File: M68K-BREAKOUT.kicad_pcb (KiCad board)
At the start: 4 copper layers, 27 parts, among them U1 68010D, U2 74ALVC164245, U3 74ALVC164245, U4 74ALVC164245, U5 74ALVC164245, U6 74LVC06

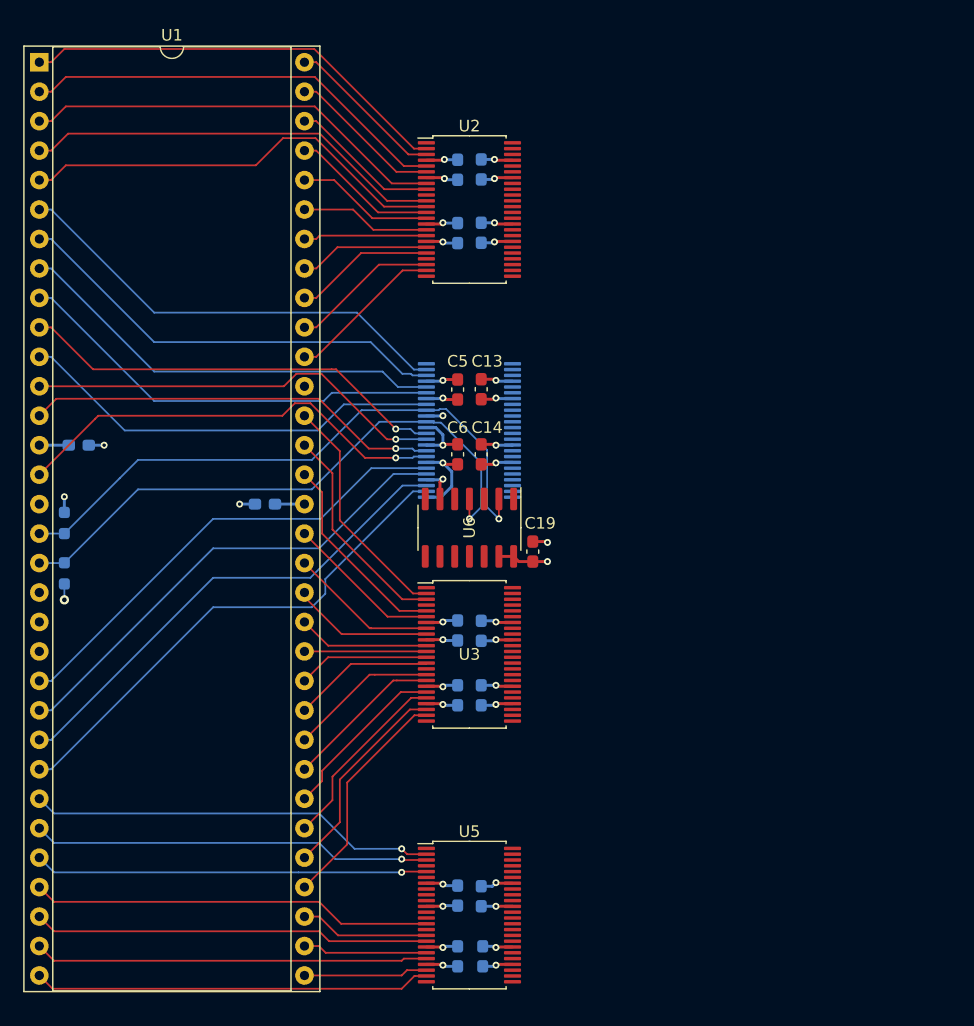
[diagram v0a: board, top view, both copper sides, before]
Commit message: complete electrical layout for the silicon centipede charmer
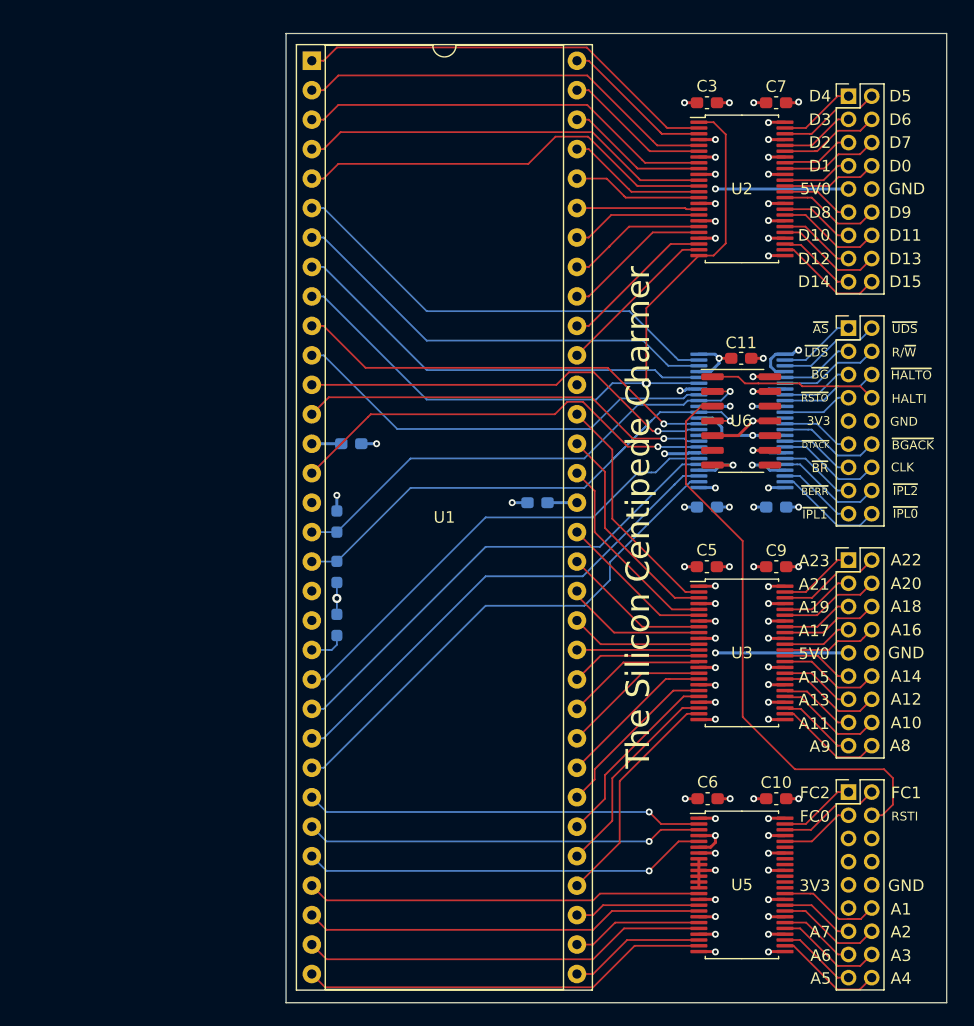
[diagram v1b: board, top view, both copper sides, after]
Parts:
- removed C12, C13, C14, C15, C16, C17, C18, C19: 100nF, Capacitor_SMD:C_0603_1608Metric_Pad1.08x0.95mm_HandSolder
- added J1: Data, Connector_PinHeader_2.00mm:PinHeader_2x09_P2.00mm_Vertical, F.Cu at (171.2, 61.1)
- added J2: Bus Signals, Connector_PinHeader_2.00mm:PinHeader_2x09_P2.00mm_Vertical, F.Cu at (171.2, 81.1)
- added J3: Address, Connector_PinHeader_2.00mm:PinHeader_2x09_P2.00mm_Vertical, F.Cu at (171.2, 101.1)
- added J4: Function Code and Lower Address, Connector_PinHeader_2.00mm:PinHeader_2x09_P2.00mm_Vertical, F.Cu at (171.2, 121.1)
- added R3: 2.2K, Resistor_SMD:R_0603_1608Metric_Pad0.98x0.95mm_HandSolder, B.Cu at (127.1, 106.7)
- C10, C11, C3, C7, C9: moved to F.Cu
- moved C7 53.1 mm to (165.0, 61.7), turned to 180 degrees
- moved C9 39.5 mm to (165.0, 101.7), turned to 180 degrees
- moved C6 36.7 mm to (159.1, 121.7), turned to 0 degrees
- moved C4 31.9 mm to (159.0, 96.5), turned to 0 degrees
- moved C8 31.9 mm to (165.0, 96.5), turned to 180 degrees
- moved C10 30.6 mm to (165.0, 121.7), turned to 180 degrees
- moved C11 27.7 mm to (162.0, 83.7), turned to 180 degrees
- moved C5 26.4 mm to (159.0, 101.7), turned to 0 degrees
- moved U6 25.2 mm to (162.0, 89.1), turned to 0 degrees
- moved U5 23.6 mm to (162.1, 129.1)
- moved U2 23.6 mm to (162.1, 69.1)
- moved U4 23.5 mm to (162.1, 89.1)
- moved C2 23.5 mm to (144.4, 96.1)
- moved U1 23.5 mm to (125.0, 58.0)
- moved U3 23.5 mm to (162.1, 109.1)
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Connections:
- C10 pad 1: +5V -> +3V3
- C7 pad 1: +5V -> +3V3
- C8 pad 1: +5V -> +3V3
- C9 pad 1: +5V -> +3V3
- U1 pad 21: +5V -> Net-(R3-Pad2)
- U2 pad 26: Net-(U2-Pad26) -> DD15
- U2 pad 27: Net-(U2-Pad27) -> DD14
- U2 pad 29: Net-(U2-Pad29) -> DD13
- U2 pad 30: Net-(U2-Pad30) -> DD12
- U2 pad 32: Net-(U2-Pad32) -> DD11
- U2 pad 33: Net-(U2-Pad33) -> DD10
- U2 pad 35: Net-(U2-Pad35) -> DD9
- U2 pad 36: Net-(U2-Pad36) -> DD8
- U2 pad 37: Net-(U2-Pad37) -> DD0
- U2 pad 38: Net-(U2-Pad38) -> DD1
- U2 pad 40: Net-(U2-Pad40) -> DD7
- U2 pad 41: Net-(U2-Pad41) -> DD2
- U2 pad 43: Net-(U2-Pad43) -> DD6
- U2 pad 44: Net-(U2-Pad44) -> DD3
- U2 pad 46: Net-(U2-Pad46) -> DD5
- U2 pad 47: Net-(U2-Pad47) -> DD4
- U3 pad 26: Net-(U3-Pad26) -> AA8
- U3 pad 27: Net-(U3-Pad27) -> AA9
- U3 pad 29: Net-(U3-Pad29) -> AA10
- U3 pad 30: Net-(U3-Pad30) -> AA11
- U3 pad 32: Net-(U3-Pad32) -> AA12
- U3 pad 33: Net-(U3-Pad33) -> AA13
- U3 pad 35: Net-(U3-Pad35) -> AA14
- U3 pad 36: Net-(U3-Pad36) -> AA15
- U3 pad 37: Net-(U3-Pad37) -> AA16
- U3 pad 38: Net-(U3-Pad38) -> AA17
- U3 pad 40: Net-(U3-Pad40) -> AA18
- U3 pad 41: Net-(U3-Pad41) -> AA19
- U3 pad 43: Net-(U3-Pad43) -> AA20
- U3 pad 44: Net-(U3-Pad44) -> AA21
- U3 pad 46: Net-(U3-Pad46) -> AA22
- U3 pad 47: Net-(U3-Pad47) -> AA23
- U4 pad 26: Net-(U4-Pad26) -> ~L_AS
- U4 pad 27: Net-(U4-Pad27) -> ~L_UDS
- U4 pad 29: Net-(U4-Pad29) -> ~L_LDS
- U4 pad 30: Net-(U4-Pad30) -> L_R~W
- U4 pad 32: Net-(U4-Pad32) -> ~L_BG
- U4 pad 33: Net-(U4-Pad33) -> ~L_HALT
- U4 pad 35: Net-(U4-Pad35) -> ~L_RESET
- U4 pad 36: GND -> Net-(U4-Pad36)
- U4 pad 37: Net-(U4-Pad37) -> ~L_DTACK
- U4 pad 38: Net-(U4-Pad38) -> ~L_BGACK
- U4 pad 40: Net-(U4-Pad40) -> ~L_BR
- U4 pad 41: Net-(U4-Pad41) -> L_CLK
- U4 pad 43: Net-(U4-Pad43) -> ~L_BERR
- U4 pad 44: Net-(U4-Pad44) -> ~L_IPL2
- U4 pad 46: Net-(U4-Pad46) -> ~L_IPL1
- U4 pad 47: Net-(U4-Pad47) -> ~L_IPL0
- U5 pad 26: LA4 -> AA4
- U5 pad 27: LA5 -> AA5
- U5 pad 29: LA3 -> AA3
- U5 pad 30: LA6 -> AA6
- U5 pad 32: LA2 -> AA2
- U5 pad 33: LA7 -> AA7
- U5 pad 35: LA1 -> AA1
- U5 pad 36: GND -> Net-(U5-Pad36)
- U5 pad 37: GND -> Net-(U5-Pad37)
- U5 pad 38: GND -> Net-(U5-Pad38)
- U5 pad 40: GND -> Net-(U5-Pad40)
- U5 pad 41: GND -> Net-(U5-Pad41)
- U5 pad 43: GND -> Net-(U5-Pad43)
- U6 pad 1: ~HALT_IN -> HALT_IN
- U6 pad 10: GND -> Net-(U6-Pad10)
- U6 pad 12: GND -> Net-(U6-Pad12)
- U6 pad 3: ~RESET_IN -> RESET_IN
- U6 pad 6: GND -> Net-(U6-Pad6)
- U6 pad 8: GND -> Net-(U6-Pad8)
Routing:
- net RESET_IN: track 0.00 -> 50.0 mm
- net GND: track 55.0 -> 100.3 mm, vias 21 -> 52
- net R~W: track 37.3 -> 65.4 mm, vias 0 -> 1
- net +5V: track 34.9 -> 51.2 mm, vias 10 -> 17
- net HALT_IN: track 0.00 -> 14.5 mm
- net ~L_UDS: track 0.00 -> 10.7 mm
- net ~HALT: track 52.6 -> 42.6 mm
- net AA1: track 0.00 -> 9.84 mm
- net AA4: track 0.00 -> 9.46 mm
- net ~L_IPL0: track 0.00 -> 9.46 mm
- net DD15: track 0.00 -> 9.46 mm
- net AA8: track 0.00 -> 9.44 mm
- net AA3: track 0.00 -> 9.23 mm
- net AA10: track 0.00 -> 9.23 mm
- net ~L_IPL2: track 0.00 -> 9.22 mm
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- added copper zone on In2.Cu, net +3V3
- added copper zone on In2.Cu, net +5V
- added copper zone on In1.Cu, net GND
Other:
- board outline added: 57 x 83.6 mm
- board text added: "3V3"
- board text added: "5V0"
- board text added: "A1"
- board text added: "A10"
- board text added: "A11"
- board text added: "A12"
- board text added: "A13"
- board text added: "A14"
- board text added: "A15"
- board text added: "A16"
- board text added: "A17"
- board text added: "A18"
- board text added: "A19"
- board text added: "A2"
- board text added: "A20"
- board text added: "A21"
- board text added: "A22"
- board text added: "A23"
- board text added: "A3"
- board text added: "A4"
- board text added: "A5"
- board text added: "A6"
- board text added: "A7"
- board text added: "A8"
- board text added: "A9"
- board text added: "CLK"
- board text added: "D0"
- board text added: "D1"
- board text added: "D10"
- board text added: "D11"
- board text added: "D12"
- board text added: "D13"
- board text added: "D14"
- board text added: "D15"
- board text added: "D2"
- board text added: "D3"
- board text added: "D4"
- board text added: "D5"
- board text added: "D6"
- board text added: "D7"
- board text added: "D8"
- board text added: "D9"
- board text added: "FC0"
- board text added: "FC1"
- board text added: "FC2"
- board text added: "GND"
- board text added: "HALTI"
- board text added: "M68K Bus Voltage Converter Revision 1.0 Designed by Nathaniel R. Lewis <hardware@nrlewis.dev>"
- board text added: "R/~W"
- board text added: "RSTI"
- board text added: "The Silicon Centipede Charmer"
- board text added: "~AS"
- board text added: "~BERR"
- board text added: "~BG"
- board text added: "~BGACK"
- board text added: "~BR"
- board text added: "~DTACK"
- board text added: "~HALTO"
- board text added: "~IPL0"
- board text added: "~IPL1"
- board text added: "~IPL2"
- board text added: "~LDS"
- board text added: "~RSTO"
- board text added: "~UDS"
